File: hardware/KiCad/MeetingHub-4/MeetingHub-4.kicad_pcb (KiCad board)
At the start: 2 copper layers, 265 x 160 mm, 74 parts, among them J1 USB-C POWER IN, J2 TRRS Notebook 1, J3 TRRS Notebook 2, J4 TRRS Notebook 3, J5 TRRS Notebook 4, J6 Headset (User), K1 Select NB1, K2 Select NB2, K3 Select NB3, K4 Select NB4, SW1 MUTE, SW2 Select NB1, SW3 Select NB2, SW4 Select NB3, SW5 Select NB4, U1 NE5532, U2 NJM4556A

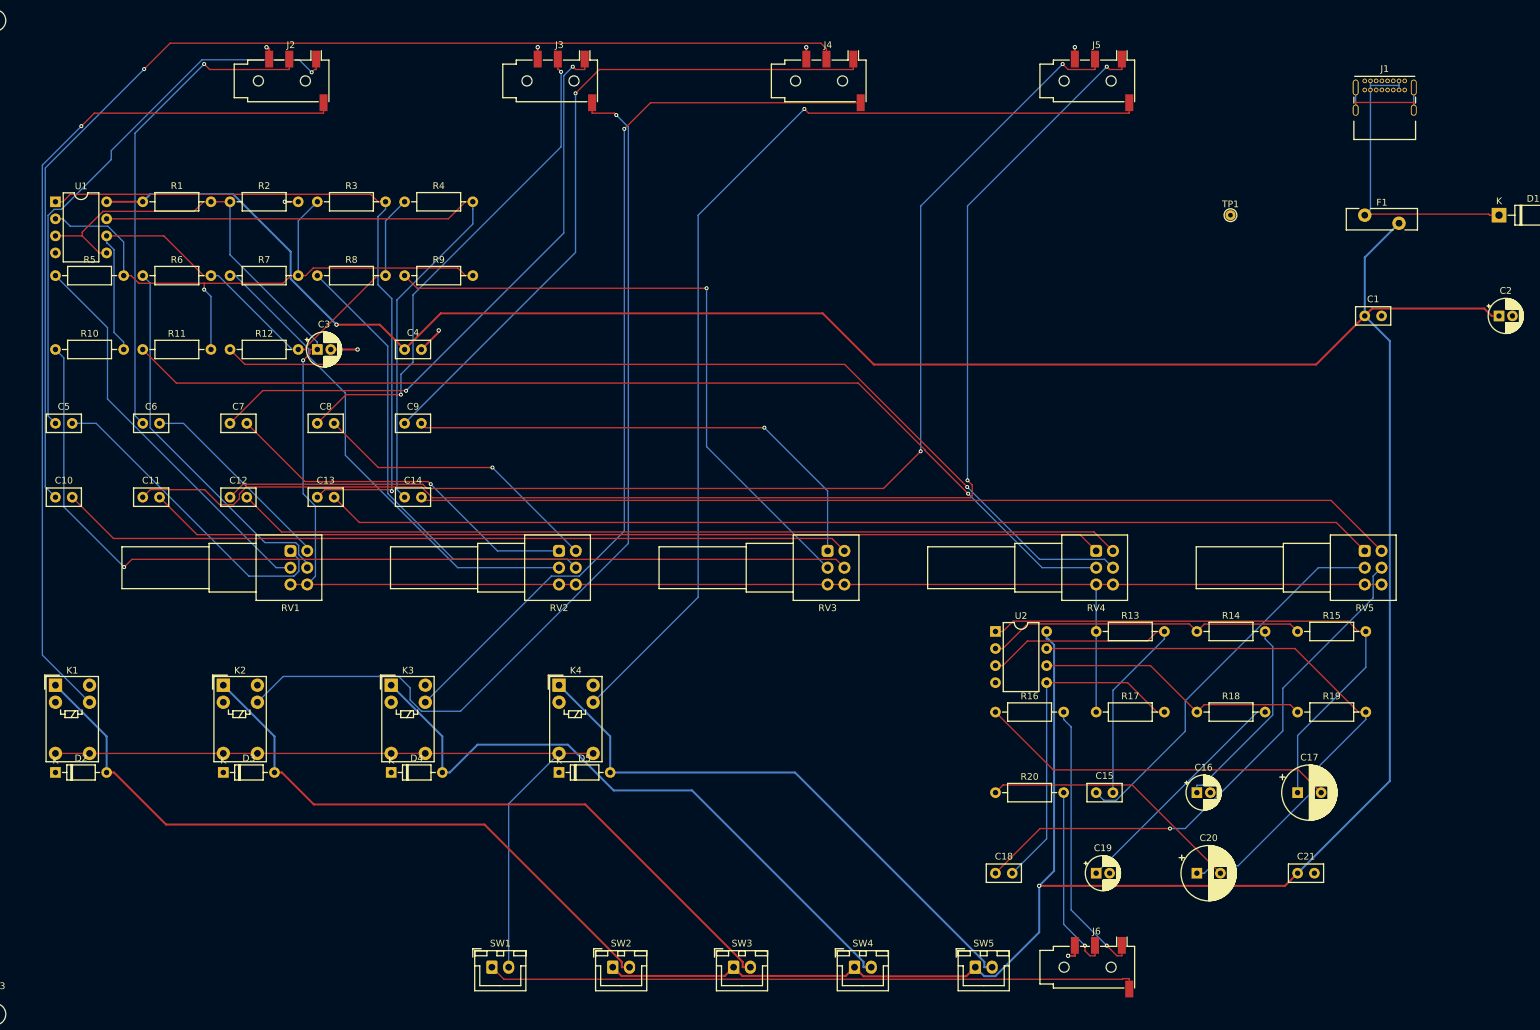
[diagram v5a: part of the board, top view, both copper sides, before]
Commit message: Re-layout mixer grid (13→15mm pitch) to fix GND plane isolation
Full redo per user request: widened the mixer grid (U1, R1-R12, C3-C14)
from 13mm to 15mm X pitch, same Y pitch and anchor, reusing the same
approach that fixed HPAMP's courtyard overlap earlier. Verified zero new
bounding-box overlaps against the rest of the board (and even resolved
2 pre-existing ones) before touching routing.

Cleared all existing tracks/vias, re-exported to Specctra DSN, and ran
Freerouting fresh: 121/121 nets routed cleanly (score 993.63). Re-applied
the established Power/RelayControl net widths (0.3mm track, 0.65mm via)
and refilled the GND zone.

This fully resolves C4 pin 2 (GND), the pad that survived every previous
stitch attempt on the old layout: added a small local detour to the
NB3_L signal trace (verified against every other net on the board,
0.64mm clearance) to open a legal path, then a short GND stub + via
through it into the main plane. Confirmed via pcbnew's own connectivity
engine (not just my approximate checks).

U1 pin 4 (GND) still needs just a bare via directly on the pad - same
as it needed before the re-layout, and same as what the last real DRC
report from the user already confirmed as sufficient (it was never
flagged as unconnected with just that via in place). My own headless
connectivity check flags it in isolation from a fresh zone fill, but
given its established track record this session of disagreeing with
real DRC specifically for this one pad, that's noted as a known
discrepancy rather than a confirmed problem - please confirm with a
real DRC run.

Validated throughout: paren balance, pcbnew connectivity
(GetUnconnectedCount), a layer-aware pad+track clearance check (only
the same 4 pre-existing, unrelated items remain - SW5 and J6 proximity,
already known from earlier in the session), and a clean
`kicad-cli pcb export gerbers`.
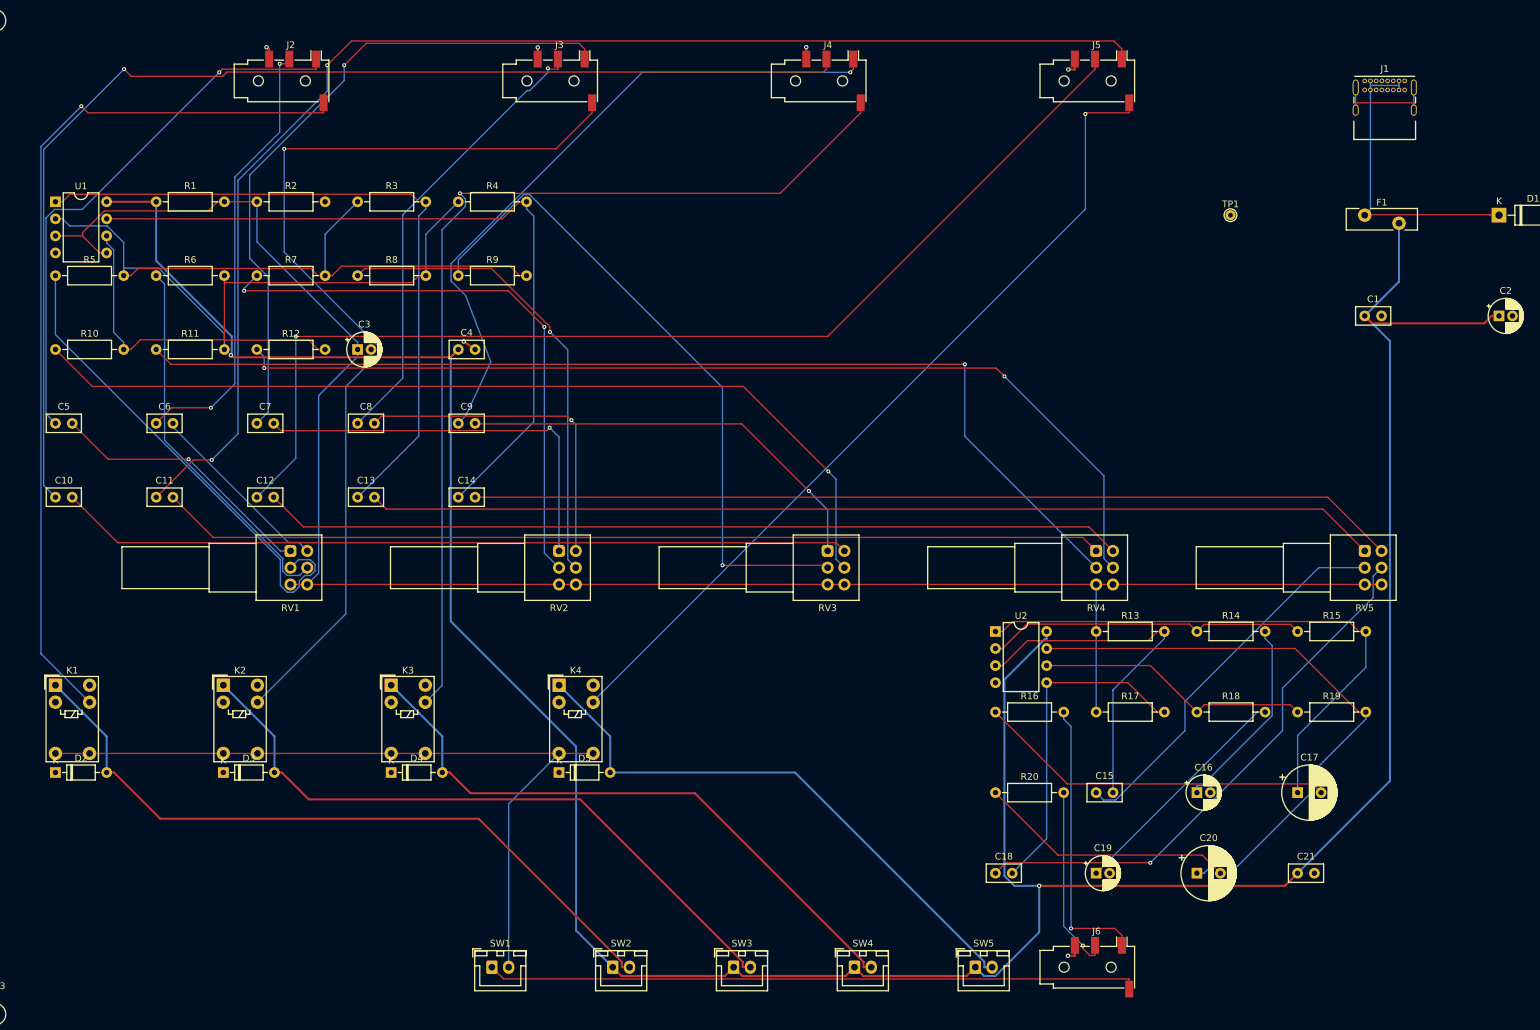
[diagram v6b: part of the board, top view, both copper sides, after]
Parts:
- moved C14 8.00 mm to (135.0, 162.0)
- moved C4 8.00 mm to (135.0, 140.0)
- moved C9 8.00 mm to (135.0, 151.0)
- moved R4 8.00 mm to (135.0, 118.0)
- moved R9 8.00 mm to (135.0, 129.0)
- moved C13 6.00 mm to (120.0, 162.0)
- moved C3 6.00 mm to (120.0, 140.0)
- moved C8 6.00 mm to (120.0, 151.0)
- moved R3 6.00 mm to (120.0, 118.0)
- moved R8 6.00 mm to (120.0, 129.0)
- moved C12 4.00 mm to (105.0, 162.0)
- moved C7 4.00 mm to (105.0, 151.0)
- moved R12 4.00 mm to (105.0, 140.0)
- moved R2 4.00 mm to (105.0, 118.0)
- moved R7 4.00 mm to (105.0, 129.0)
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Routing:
- net +5V_AUDIO: track 490.9 -> 460.1 mm
- net NB4_MIC: track 151.6 -> 126.1 mm
- net Net-(U1A--): track 92.9 -> 113.0 mm, vias 1 -> 0
- net Net-(U1B--): track 83.6 -> 102.2 mm
- net NB4_R: track 179.3 -> 163.4 mm, vias 2 -> 1
- net Net-(R7-Pad1): track 73.1 -> 86.7 mm, vias 0 -> 2
- net Net-(R5-Pad1): track 59.2 -> 72.8 mm
- net NB2_L: track 90.3 -> 100.0 mm, vias 2 -> 1
- net Net-(C9-Pad2): track 73.6 -> 64.0 mm
- net Net-(C14-Pad2): track 146.3 -> 138.3 mm
- net Net-(C14-Pad1): track 104.7 -> 112.7 mm
- net NB3_MIC: track 136.9 -> 144.8 mm
- net GND: track 19.8 -> 12.7 mm, vias 9 -> 7
- net Net-(R10-Pad1): track 144.9 -> 138.0 mm
- net Net-(C5-Pad2): track 47.0 -> 40.4 mm, vias 0 -> 1
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
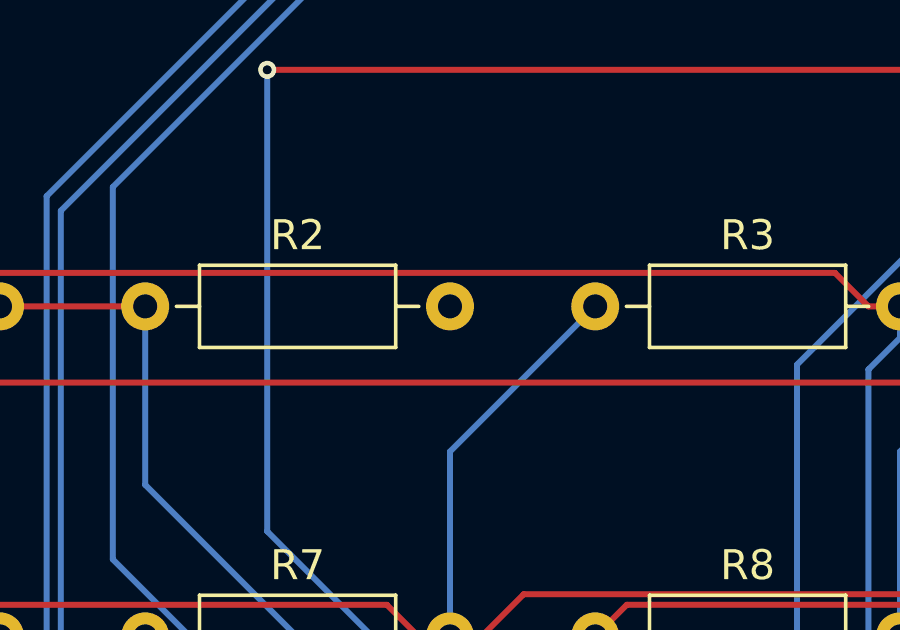
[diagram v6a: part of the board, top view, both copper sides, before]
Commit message: Fix R2 unconnected pad and starved-thermal on C1/C3 (real DRC)
Real DRC on the re-layouted board confirmed U1 pin 4 and C4 pin 2 are
both fine (matching the last commit's prediction) and surfaced 2 new
issues from the fresh routing pass:

- R2 pin 2 (GND) was fully unconnected in its new grid position. Fixed
  with a trivial 0.4mm stub + via straight down into the main plane
  (0.87mm/1.09mm clearance to everything else).

- C1 pin 2 and C3 pin 2 (GND) had [starved_thermal] errors - the zone
  filler could only route 1 thermal-relief spoke where 2 are required,
  in both cases due to nearby signal-trace congestion. Rather than
  fight the zone filler for more spoke room, set both pads' zone
  connection to ZONE_CONNECTION_FULL (solid fill instead of thermal
  relief) - this is the standard KiCad fix for this exact warning, since
  a solid connection has no spokes to be short on.

Validated: paren balance, pcbnew connectivity, layer-aware clearance
check (only the same 4 pre-existing SW5/J6 items remain), and a clean
kicad-cli pcb export gerbers. Please re-run DRC to confirm.
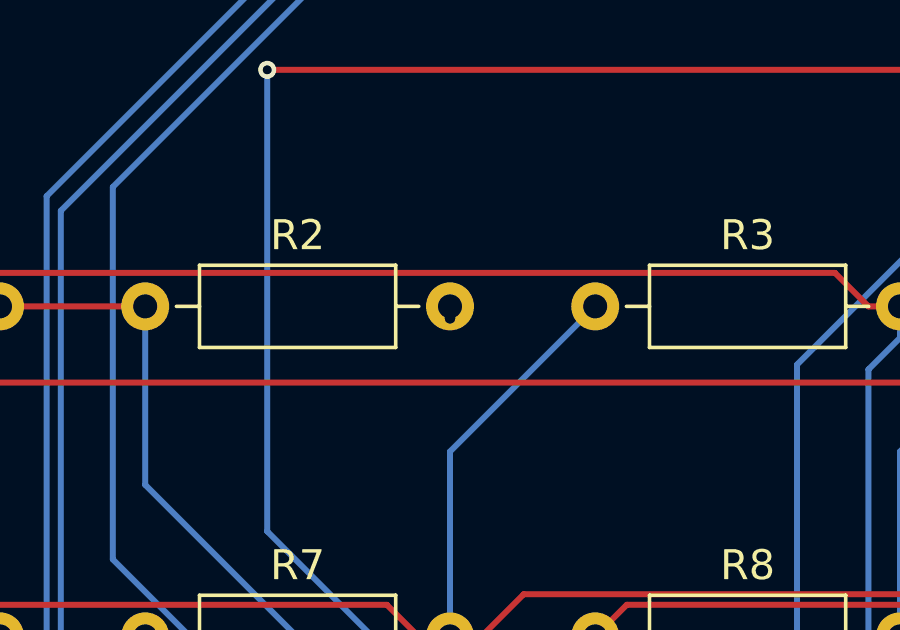
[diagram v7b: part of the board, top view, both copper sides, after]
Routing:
- net GND: track 12.7 -> 13.1 mm, vias 7 -> 8
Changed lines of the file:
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@@
       (net 1 "+5V_AUDIO") (pintype "passive"))
     (pad "2" thru_hole circle (at 2.5 0) (size 1.6 1.6) (drill 0.8) (layers "*.Cu" "*.Mask")
-      (net 2 "GND") (pintype "passive"))
+      (net 2 "GND") (pintype "passive") (zone_connect 2))
     (model "${KICAD6_3DMODEL_DIR}/Capacitor_THT.3dshapes/C_Disc_D5.0mm_W2.5mm_P2.50mm.wrl"
       (offset (xyz 0 0 0))
@@
       (net 3 "VBIAS") (pintype "passive"))
     (pad "2" thru_hole circle (at 2 0) (size 1.6 1.6) (drill 0.8) (layers "*.Cu" "*.Mask")
-      (net 2 "GND") (pintype "passive"))
+      (net 2 "GND") (pintype "passive") (zone_connect 2))
     (model "${KICAD6_3DMODEL_DIR}/Capacitor_THT.3dshapes/CP_Radial_D5.0mm_P2.00mm.wrl"
       (offset (xyz 0 0 0))
@@
   (segment (start 137.5 140) (end 135.8 138.8) (width 0.3) (layer "F.Cu") (net 2))
   (segment (start 106.6359 95.1981) (end 106.825 95.1981) (width 0.3) (layer "F.Cu") (net 2))
+  (segment (start 115.16 118) (end 115.16 118.4) (width 0.3) (layer "F.Cu") (net 2))
   (segment (start 226.825 228.75) (end 226.825 230.3019) (width 0.3) (layer "F.Cu") (net 2))
   (segment (start 146.825 95.015) (end 146.825 96.75) (width 0.3) (layer "F.Cu") (net 2))
@@
   (via (at 106.43 94.9922) (size 0.65) (drill 0.35) (layers "F.Cu" "B.Cu") (net 2))
   (via (at 225.7936 230.3019) (size 0.65) (drill 0.35) (layers "F.Cu" "B.Cu") (net 2))
+  (via (at 115.16 118.4) (size 0.65) (drill 0.35) (layers "F.Cu" "B.Cu") (net 2))
   (via (at 75 125.62) (size 0.65) (drill 0.35) (layers "F.Cu" "B.Cu") (net 2))
   (via (at 225.8417 98.3019) (size 0.65) (drill 0.35) (layers "F.Cu" "B.Cu") (net 2))

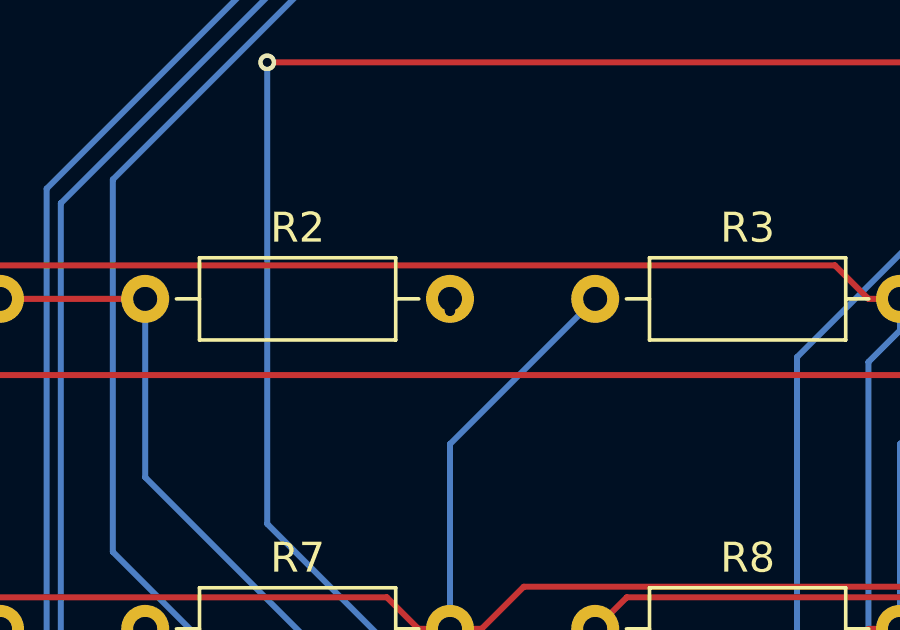
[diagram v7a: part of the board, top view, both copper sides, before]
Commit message: Fix hole-to-hole violation on R2's GND stitch via
The R2 pin 2 stitch from the last commit placed its via only 0.4mm from
R2's own pad, but R2 uses a 0.8mm drill and the via a 0.35mm drill -
their holes were touching (0.0mm actual vs 0.2495mm minimum required),
flagged as 2 [hole_near_hole] errors. Moved the via to 0.9mm from the
pad (0.325mm hole-to-hole clearance), same direction, still comfortably
inside the main GND plane and clear of everything else.

Validated: paren balance, clearance check (only the same 4 pre-existing
SW5/J6 items remain), clean kicad-cli pcb export gerbers.
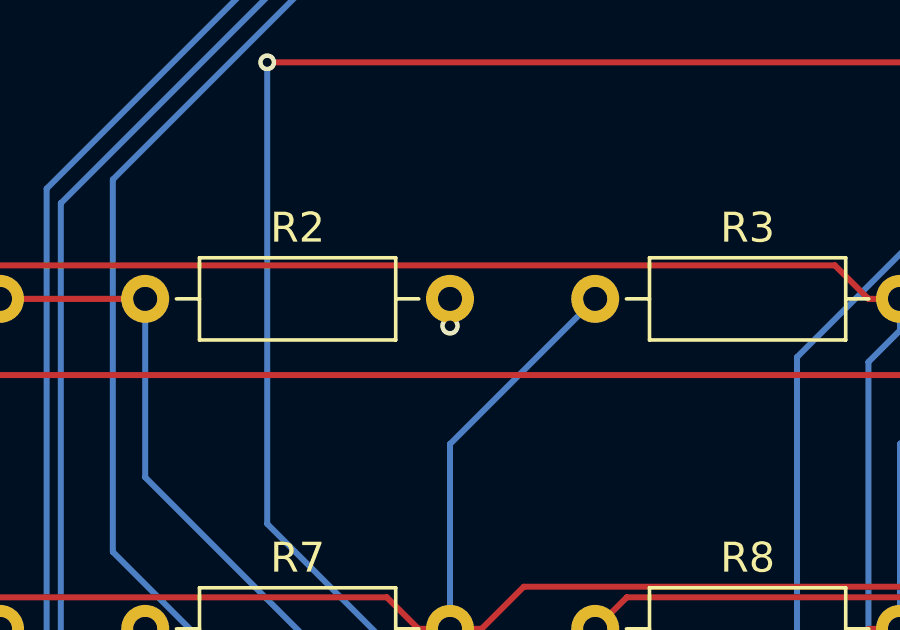
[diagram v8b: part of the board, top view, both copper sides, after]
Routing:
- net GND: track 13.1 -> 13.6 mm
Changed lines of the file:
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@@
   (segment (start 137.5 140) (end 135.8 138.8) (width 0.3) (layer "F.Cu") (net 2))
   (segment (start 106.6359 95.1981) (end 106.825 95.1981) (width 0.3) (layer "F.Cu") (net 2))
-  (segment (start 115.16 118) (end 115.16 118.4) (width 0.3) (layer "F.Cu") (net 2))
   (segment (start 226.825 228.75) (end 226.825 230.3019) (width 0.3) (layer "F.Cu") (net 2))
   (segment (start 146.825 95.015) (end 146.825 96.75) (width 0.3) (layer "F.Cu") (net 2))
   (segment (start 226.825 230.3019) (end 225.7936 230.3019) (width 0.3) (layer "F.Cu") (net 2))
   (segment (start 186.825 94.9894) (end 186.825 96.75) (width 0.3) (layer "F.Cu") (net 2))
+  (segment (start 115.16 118) (end 115.16 118.9) (width 0.3) (layer "F.Cu") (net 2))
   (segment (start 106.43 94.9922) (end 106.6359 95.1981) (width 0.3) (layer "F.Cu") (net 2))
   (segment (start 226.825 96.75) (end 226.825 98.3019) (width 0.3) (layer "F.Cu") (net 2))
+  (via (at 115.16 118.9) (size 0.65) (drill 0.35) (layers "F.Cu" "B.Cu") (net 2))
   (via (at 135.8 138.8) (size 0.65) (drill 0.35) (layers "F.Cu" "B.Cu") (net 2))
   (via (at 146.825 95.015) (size 0.65) (drill 0.35) (layers "F.Cu" "B.Cu") (net 2))
@@
   (via (at 106.43 94.9922) (size 0.65) (drill 0.35) (layers "F.Cu" "B.Cu") (net 2))
   (via (at 225.7936 230.3019) (size 0.65) (drill 0.35) (layers "F.Cu" "B.Cu") (net 2))
-  (via (at 115.16 118.4) (size 0.65) (drill 0.35) (layers "F.Cu" "B.Cu") (net 2))
   (via (at 75 125.62) (size 0.65) (drill 0.35) (layers "F.Cu" "B.Cu") (net 2))
   (via (at 225.8417 98.3019) (size 0.65) (drill 0.35) (layers "F.Cu" "B.Cu") (net 2))
